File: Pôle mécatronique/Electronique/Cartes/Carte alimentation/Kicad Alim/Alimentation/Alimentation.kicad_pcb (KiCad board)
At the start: 2 copper layers, 11 parts, among them J1 Conn_01x04, J2 Conn_01x04, J3 Conn_01x04, J4 Conn_01x05, J5 Conn_02x03_Odd_Even, J6 Conn_01x05, K1 G5LE-1, Q1 2N7002, U1 TSR_2-2450, U2 TSR_2-2450, U3 TSR_2-24120

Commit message: Update alim
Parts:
- added D1: D, Diode_THT:D_DO-15_P12.70mm_Horizontal, F.Cu at (177.3, 89.4)
- added J7: Conn_02x10_Odd_Even, Connector_PinSocket_2.54mm:PinSocket_2x10_P2.54mm_Vertical, F.Cu at (131.8, 64.3)
- J5: footprint Connector_JST:JST_PH_B4B-PH-K_1x04_P2.00mm_Vertical -> Connector_Hirose:Hirose_DF11-6DP-2DSA_2x03_P2.00mm_Vertical
- Q1: value 2N7002 -> BSS138
- moved U2 54.2 mm to (140.5, 91.9), turned to 90 degrees
- moved J3 54.0 mm to (148.1, 42.4), turned to 270 degrees
- moved U1 52.1 mm to (129.3, 91.9), turned to 90 degrees
- moved J4 48.4 mm to (127.8, 42.4), turned to 270 degrees
- moved Q1 48.3 mm to (153.2, 74.2)
- moved J5 48.2 mm to (122.7, 73.4), turned to 180 degrees
- moved J2 43.5 mm to (157.0, 42.4), turned to 270 degrees
- moved J6 41.5 mm to (135.4, 42.4), turned to 270 degrees
- moved U3 28.0 mm to (151.9, 92.2), turned to 90 degrees
- moved J1 26.8 mm to (165.9, 42.4), turned to 270 degrees
- moved K1 20.1 mm to (165.9, 78.0)
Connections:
- J4 pad 4: 12Vout1 -> 5Vout4
- J6 pad 4: 12Vout2 -> 5Vout5
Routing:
- net GND: track 0.00 -> 135.1 mm
- net can_H: track 0.00 -> 95.1 mm
- net can_L: track 0.00 -> 90.8 mm
- net 5V: track 0.00 -> 71.5 mm
- net Net-(J7-Pad2): track 0.00 -> 49.6 mm
- net Vbatt: track 0.00 -> 43.2 mm
- net cmd_relais: track 0.00 -> 33.3 mm
- net Net-(J7-Pad16): track 0.00 -> 32.2 mm
- net 5VRPI: track 0.00 -> 30.4 mm
- net Net-(D1-Pad2): track 0.00 -> 27.9 mm
- net 5Vout1: track 0.00 -> 25.6 mm
- net VbattProtected: track 0.00 -> 21.9 mm
- net 5Vout4: track 0.00 -> 21.0 mm
- net 5Vout2: track 0.00 -> 21.0 mm
- net 5Vout3: track 0.00 -> 18.4 mm
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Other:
- board outline added: 71.1 x 66 mm

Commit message: Update alim
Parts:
- added J8: Conn_01x02, Connector_AMASS:AMASS_XT60-F_1x02_P7.20mm_Vertical, F.Cu at (116.3, 107.2)
- added R1: 6000, Resistor_THT:R_Axial_DIN0207_L6.3mm_D2.5mm_P10.16mm_Horizontal, F.Cu at (104.3, 60.8)
- added REF**: MountingHole_3.2mm_M3, MountingHole:MountingHole_3.2mm_M3, F.Cu at (90.9, 107.2)
- added REF**: MountingHole_3.2mm_M3, MountingHole:MountingHole_3.2mm_M3, F.Cu at (149.4, 107.2)
- added REF**: MountingHole_3.2mm_M3, MountingHole:MountingHole_3.2mm_M3, F.Cu at (90.9, 38.6)
- added REF**: MountingHole_3.2mm_M3, MountingHole:MountingHole_3.2mm_M3, F.Cu at (149.4, 38.6)
- Q1: moved to B.Cu
- moved D1 71.3 mm to (108.7, 69.7), turned to 180 degrees
- moved K1 63.6 mm to (102.4, 75.4)
- moved Q1 48.6 mm to (105.5, 64.6), turned to 270 degrees
- moved J5 35.4 mm to (97.9, 48.1), turned to 270 degrees
- moved U3 33.7 mm to (118.2, 91.9)
- moved J6 30.1 mm to (105.5, 46.2)
- moved J2 23.2 mm to (134.1, 46.2)
- moved J3 23.2 mm to (125.2, 46.2)
- moved J1 23.2 mm to (143.0, 46.2)
- moved J7 16.6 mm to (117.6, 72.9)
- moved J4 15.1 mm to (113.2, 46.2)
- moved U1 11.2 mm to (140.5, 91.9)
- moved U2 10.8 mm to (129.7, 91.9)
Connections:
- J5 pad 3: cmd_relais -> Net-(J5-Pad3)
- J5 pad 4: Net-(J5-Pad4) -> cmd_relais
- Q1 pad 1: cmd_relais -> Net-(Q1-Pad1)
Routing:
- net GND: track 135.1 -> 0.00 mm
- net 5VRPI: track 30.4 -> 90.3 mm, vias 0 -> 2
- net Net-(J7-Pad2): track 49.6 -> 14.2 mm
- net Vbatt: track 43.2 -> 69.1 mm
- net cmd_relais: track 33.3 -> 12.2 mm
- net can_H: track 95.1 -> 74.7 mm
- net 5V: track 71.5 -> 52.5 mm, vias 0 -> 2
- net Net-(J7-Pad16): track 32.2 -> 13.5 mm
- net can_L: track 90.8 -> 74.2 mm
- net 5Vout5: track 16.8 -> 28.6 mm
- net VbattProtected: track 21.9 -> 10.8 mm
- net 12Vout2: track 15.3 -> 24.3 mm
- net Net-(D1-Pad2): track 27.9 -> 19.2 mm
- net 5Vout4: track 21.0 -> 26.2 mm
- net 12Vout1: track 16.6 -> 21.6 mm, vias 0 -> 2
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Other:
- board size 71.1 x 66 mm -> 68.6 x 78.7 mm

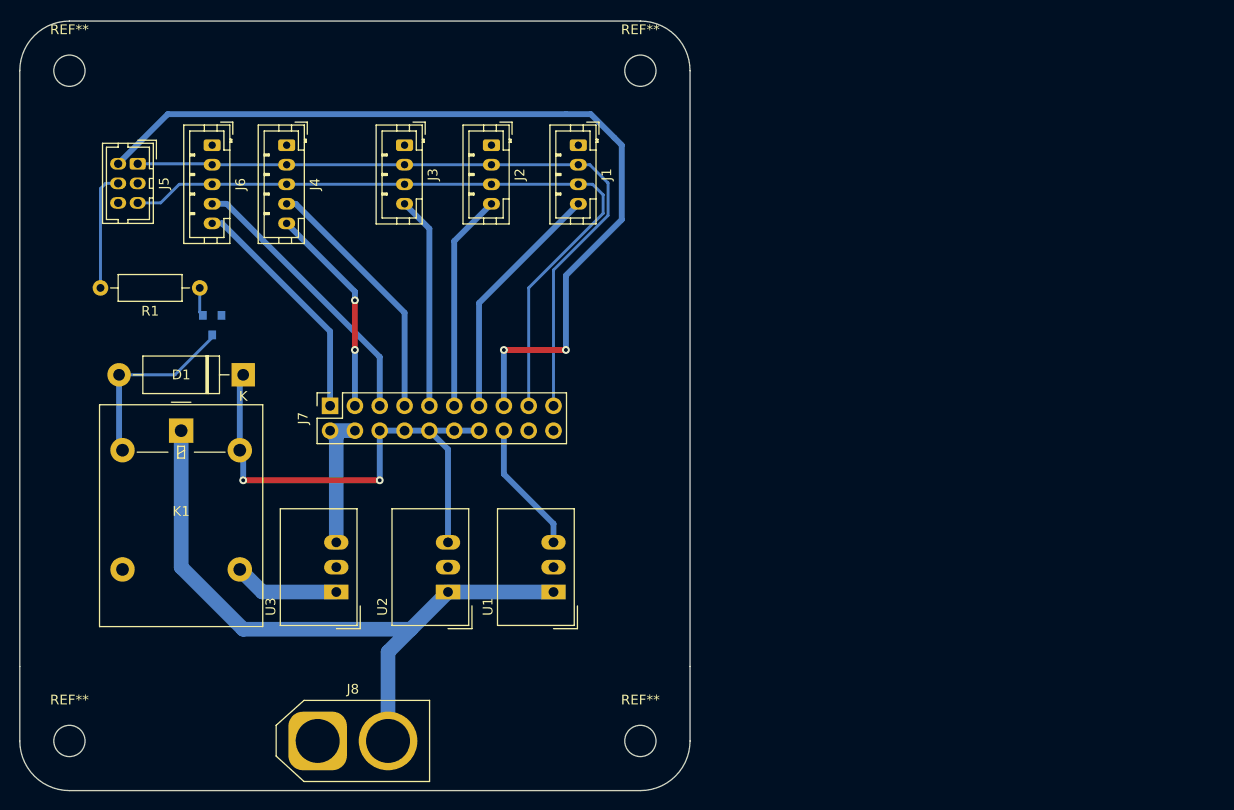
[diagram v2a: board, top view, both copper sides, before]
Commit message: Update Alim
Manque fusible
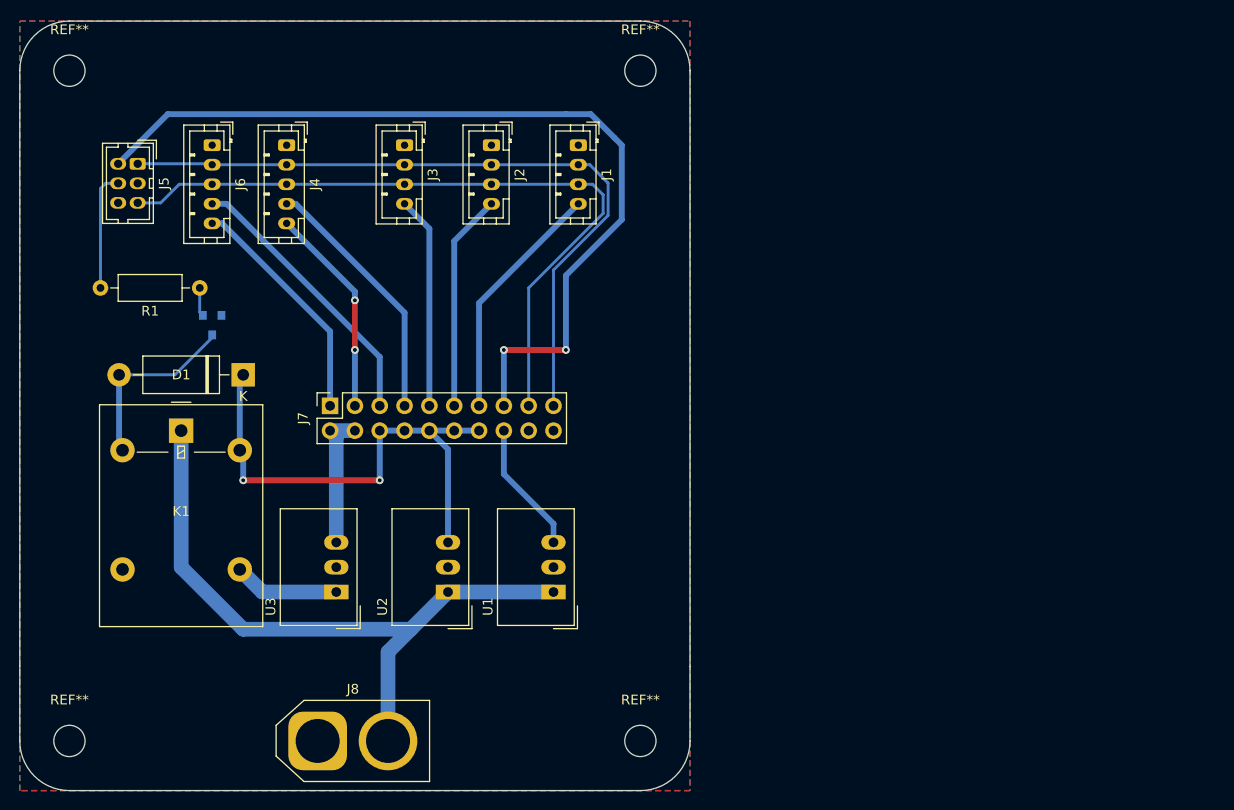
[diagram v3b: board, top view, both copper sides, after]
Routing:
- added copper zone on B.Cu, net GND
- added copper zone on F.Cu, net GND

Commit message: Update alim
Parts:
- added G***: LOGO, Logos:logoRobotechNancy10x10, F.Cu at (140.5, 60.2)
- added G***: LOGO, Logos:logoRobotechNancy10x10, B.Cu at (140.5, 60.2)
- added J9: Conn_01x02, Connector_AMASS:AMASS_XT60-F_1x02_P7.20mm_Vertical, F.Cu at (129.5, 107.2)
- Q1: value BSS138 -> BD135; footprint Package_TO_SOT_SMD:SOT-23 -> Package_TO_SOT_THT:TO-126-3_Vertical; moved to F.Cu
- R1: value 6000 -> 18000
- moved J8 11.2 mm to (105.1, 107.2)
- moved Q1 6.36 mm to (99.2, 64.4), turned to 0 degrees
- moved R1 1.91 mm to (104.3, 58.9)
- moved J4 0.64 mm to (113.8, 46.2)
- renumbered J6 to J5, J5 to J6
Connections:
- J6 pad 3: Net-(J5-Pad3) -> can_L
- J6 pad 5: can_L -> unconnected-(J6-Pad5)
- J7 pad 20: Net-(J7-Pad20) -> unconnected-(J7-Pad20)
- K1 pad 3: Net-(K1-Pad3) -> unconnected-(K1-Pad3)
- Q1 pad 1: Net-(Q1-Pad1) -> GND
- Q1 pad 2: GND -> Net-(D1-Pad2)
- Q1 pad 3: Net-(D1-Pad2) -> Net-(R1-Pad1)
- R1 pad 1: Net-(Q1-Pad1) -> Net-(R1-Pad1)
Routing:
- net Vbatt: track 69.1 -> 84.8 mm
- net Net-(R1-Pad1): track 0.00 -> 5.45 mm
- net Net-(Q1-Pad1): track 2.94 -> 0.00 mm
- net Net-(D1-Pad2): track 19.2 -> 17.1 mm
- net cmd_relais: track 12.2 -> 10.3 mm
- net can_L: track 74.2 -> 73.5 mm
- net 5Vout4: track 26.2 -> 25.6 mm
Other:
- net class Default removed
- board text added: "+"
- board text added: "-"
- board text added: "-12V"
- board text added: "-5V"
- board text added: "-5VRPI"
- board text added: "12V"
- board text added: "5V"
- board text added: "5V-12V"
- board text added: "5VRPI"
- board text added: "Batterie"
- board text added: "Carte de mesure"
- board text added: "GND"
- board text added: "ROBOTECH NANCY"
- board text added: "Relais"
- board text added: "canH"
- board text added: "canL"

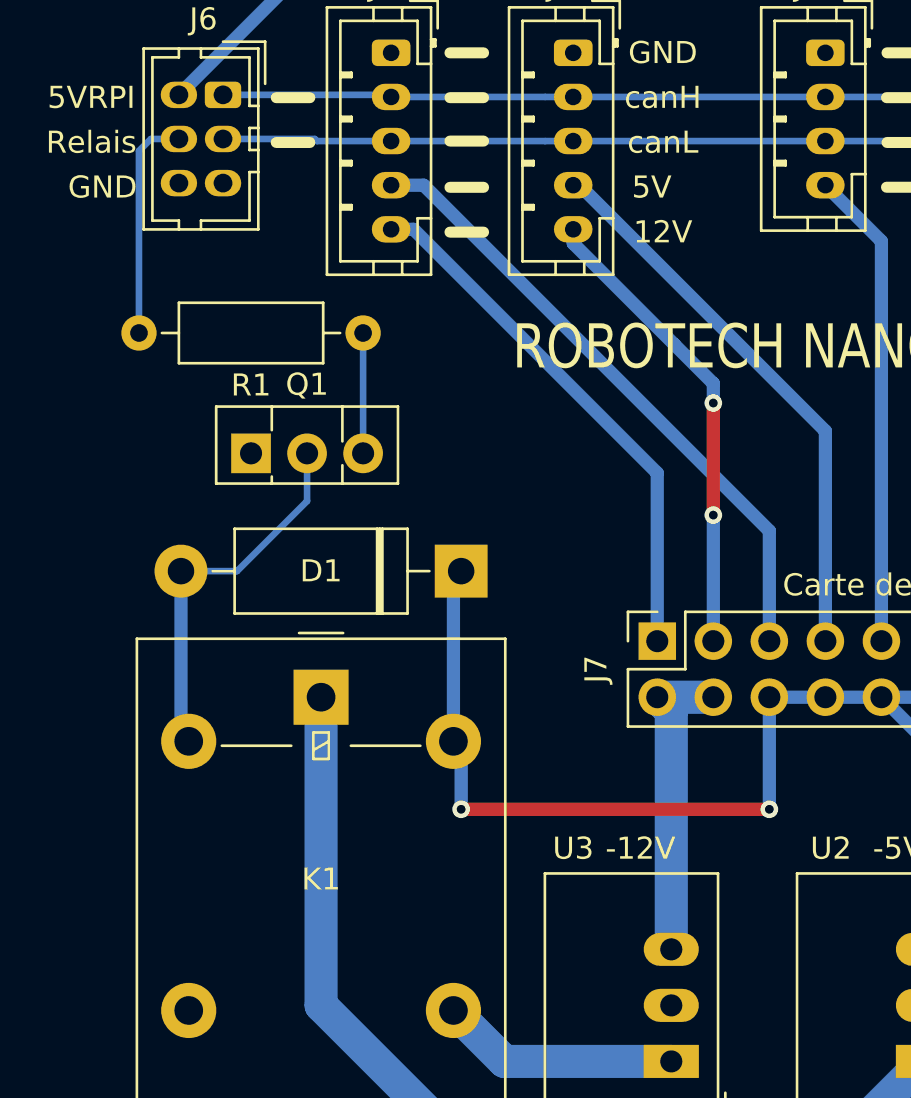
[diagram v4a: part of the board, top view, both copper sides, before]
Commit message: Update Alim
Transistor alimenté en 12V
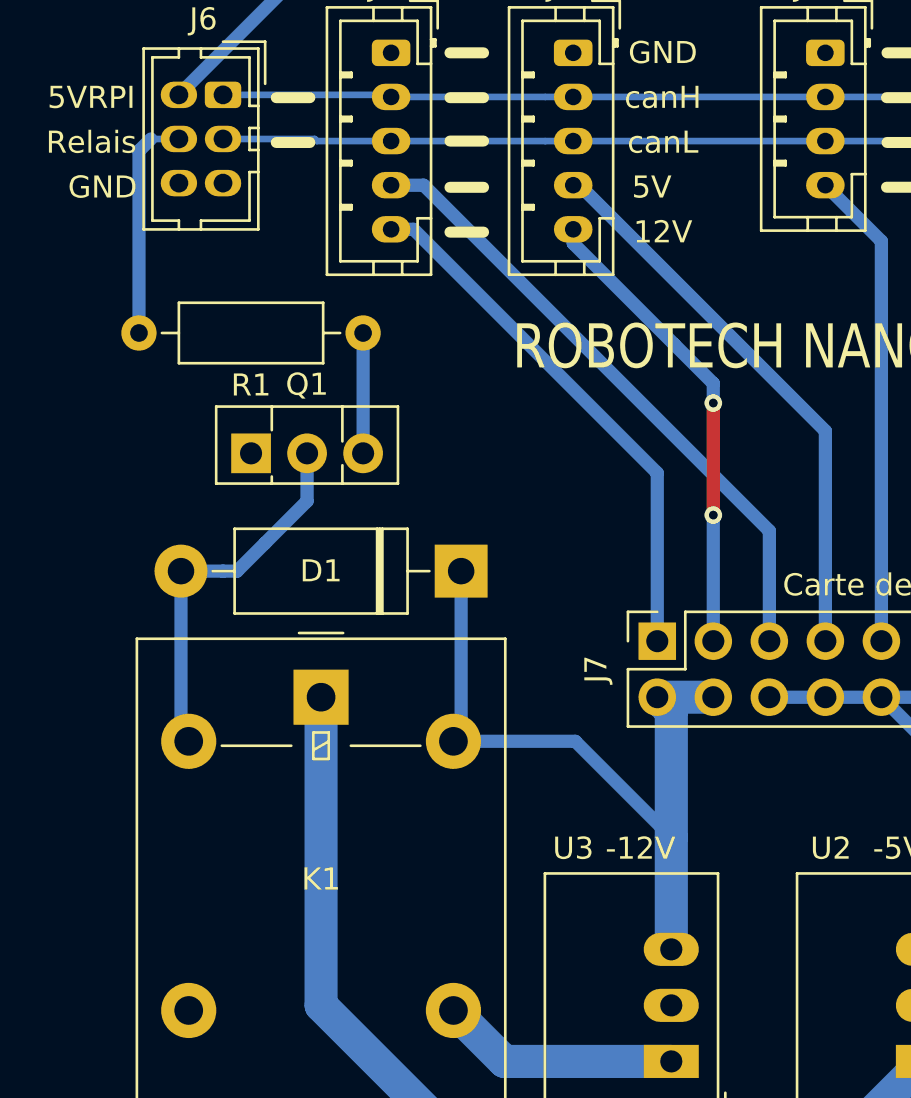
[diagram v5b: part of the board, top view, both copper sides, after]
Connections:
- D1 pad 1: 5V -> 12V
- J7 pad 2: Net-(J7-Pad2) -> 12V
- J7 pad 4: Net-(J7-Pad2) -> 12V
- K1 pad 5: 5V -> 12V
- U3 pad 3: Net-(J7-Pad2) -> 12V
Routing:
- net 12V: track 0.00 -> 34.3 mm
- net 5V: track 52.5 -> 22.4 mm, vias 2 -> 0
- net Net-(J7-Pad2): track 14.2 -> 0.00 mm
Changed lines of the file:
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@@
   (net 13 "Net-(D1-Pad2)")
   (net 14 "Vbatt")
-  (net 15 "Net-(J7-Pad2)")
+  (net 15 "12V")
   (net 16 "5Vout4")
   (net 17 "5Vout5")
@@
   (net 20 "unconnected-(K1-Pad3)")
   (net 21 "unconnected-(J6-Pad5)")
-  (net 22 "Net-(R1-Pad1)")
+  (net 22 "Net-(Q1-Pad3)")
   (footprint "Connector_JST:JST_PH_B4B-PH-K_1x04_P2.00mm_Vertical" (layer "F.Cu")
     (at 143.002 46.228 -90)
@@
       (net 12 "VbattProtected") (pintype "passive"))
     (pad "5" thru_hole oval locked (at 6 2) (size 2.5 2.5) (drill 1.3) (layers *.Cu *.Mask)
-      (net 11 "5V") (pintype "passive"))
+      (net 15 "12V") (pintype "passive"))
     (model "${KICAD6_3DMODEL_DIR}/Relay_THT.3dshapes/Relay_SPDT_Omron-G5LE-1.wrl"
       (offset (xyz 0 0 0))
@@
       (net 4 "GND") (pinfunction "GND") (pintype "power_in"))
     (pad "3" thru_hole oval locked (at 5.08 0 90) (size 1.5 2.5) (drill 1) (layers *.Cu *.Mask)
-      (net 15 "Net-(J7-Pad2)") (pinfunction "Vout") (pintype "power_out"))
+      (net 15 "12V") (pinfunction "Vout") (pintype "power_out"))
     (model "${KICAD6_3DMODEL_DIR}/Converter_DCDC.3dshapes/Converter_DCDC_TRACO_TSR-1_THT.wrl"
       (offset (xyz 0 0 0))
@@
       (net 10 "12Vout2") (pinfunction "Pin_1") (pintype "passive"))
     (pad "2" thru_hole oval locked (at -2.54 0 90) (size 1.7 1.7) (drill 1) (layers *.Cu *.Mask)
-      (net 15 "Net-(J7-Pad2)") (pinfunction "Pin_2") (pintype "passive"))
+      (net 15 "12V") (pinfunction "Pin_2") (pintype "passive"))
     (pad "3" thru_hole oval locked (at 0 2.54 90) (size 1.7 1.7) (drill 1) (layers *.Cu *.Mask)
       (net 7 "12Vout1") (pinfunction "Pin_3") (pintype "passive"))
     (pad "4" thru_hole oval locked (at -2.54 2.54 90) (size 1.7 1.7) (drill 1) (layers *.Cu *.Mask)
-      (net 15 "Net-(J7-Pad2)") (pinfunction "Pin_4") (pintype "passive"))
+      (net 15 "12V") (pinfunction "Pin_4") (pintype "passive"))
     (pad "5" thru_hole oval locked (at 0 5.08 90) (size 1.7 1.7) (drill 1) (layers *.Cu *.Mask)
       (net 17 "5Vout5") (pinfunction "Pin_5") (pintype "passive"))
@@
     (fp_line (start 2.55 1.8) (end 10.15 1.8) (layer "F.Fab") (width 0.1))
     (pad "1" thru_hole rect locked (at 0 0 180) (size 2.4 2.4) (drill 1.2) (layers *.Cu *.Mask)
-      (net 11 "5V") (pinfunction "K") (pintype "passive"))
+      (net 15 "12V") (pinfunction "K") (pintype "passive"))
     (pad "2" thru_hole oval locked (at 12.7 0 180) (size 2.4 2.4) (drill 1.2) (layers *.Cu *.Mask)
       (net 13 "Net-(D1-Pad2)") (pinfunction "A") (pintype "passive"))
@@
     (fp_line (start 8.23 1.25) (end 8.23 -1.25) (layer "F.Fab") (width 0.1))
     (pad "1" thru_hole circle locked (at 0 0 180) (size 1.6 1.6) (drill 0.8) (layers *.Cu *.Mask)
-      (net 22 "Net-(R1-Pad1)") (pintype "passive"))
+      (net 22 "Net-(Q1-Pad3)") (pintype "passive"))
     (pad "2" thru_hole oval locked (at 10.16 0 180) (size 1.6 1.6) (drill 0.8) (layers *.Cu *.Mask)
       (net 8 "cmd_relais") (pintype "passive"))
@@
       (net 13 "Net-(D1-Pad2)") (pinfunction "C") (pintype "passive"))
     (pad "3" thru_hole oval locked (at 5.08 0) (size 1.8 1.8) (drill 1) (layers *.Cu *.Mask)
-      (net 22 "Net-(R1-Pad1)") (pinfunction "B") (pintype "input"))
+      (net 22 "Net-(Q1-Pad3)") (pinfunction "B") (pintype "input"))
     (model "${KICAD6_3DMODEL_DIR}/Package_TO_SOT_THT.3dshapes/TO-126-3_Vertical.wrl"
       (offset (xyz 0 0 0))
@@
   (segment (start 120.142 72.898) (end 120.142 67.183) (width 0.6) (layer "B.Cu") (net 7))
   (segment (start 118.3645 59.4355) (end 113.792 54.863) (width 0.6) (layer "B.Cu") (net 7))
-  (segment (start 94.107 58.928) (end 94.107 50.673) (width 0.3) (layer "B.Cu") (net 8))
   (segment (start 94.647 50.133) (end 95.917 50.133) (width 0.3) (layer "B.Cu") (net 8))
-  (segment (start 94.107 50.673) (end 94.647 50.133) (width 0.3) (layer "B.Cu") (net 8))
+  (segment (start 94.107 50.673) (end 94.107 58.928) (width 0.6) (layer "B.Cu") (net 8))
+  (segment (start 94.647 50.133) (end 94.107 50.673) (width 0.6) (layer "B.Cu") (net 8))
   (segment (start 141.732 67.183) (end 135.382 67.183) (width 0.6) (layer "F.Cu") (net 9))
   (via (at 135.382 67.183) (size 0.8) (drill 0.4) (layers "F.Cu" "B.Cu") (net 9))
@@
   (segment (start 117.602 72.898) (end 117.602 65.278) (width 0.6) (layer "B.Cu") (net 10))
   (segment (start 106.552 54.228) (end 105.537 54.228) (width 0.6) (layer "B.Cu") (net 10))
-  (segment (start 108.712 80.518) (end 122.682 80.518) (width 0.6) (layer "F.Cu") (net 11))
-  (via (at 122.682 80.518) (size 0.8) (drill 0.4) (layers "F.Cu" "B.Cu") (net 11))
-  (via (at 108.712 80.518) (size 0.8) (drill 0.4) (layers "F.Cu" "B.Cu") (net 11))
   (segment (start 125.222 75.438) (end 122.682 75.438) (width 0.6) (layer "B.Cu") (net 11))
   (segment (start 132.842 75.438) (end 130.302 75.438) (width 0.6) (layer "B.Cu") (net 11))
   (segment (start 127.762 75.438) (end 125.222 75.438) (width 0.6) (layer "B.Cu") (net 11))
-  (segment (start 108.362 77.438) (end 108.362 70.073) (width 0.6) (layer "B.Cu") (net 11))
-  (segment (start 108.712 77.788) (end 108.362 77.438) (width 0.6) (layer "B.Cu") (net 11))
-  (segment (start 108.362 70.073) (end 108.712 69.723) (width 0.6) (layer "B.Cu") (net 11))
   (segment (start 129.667 77.343) (end 127.762 75.438) (width 0.6) (layer "B.Cu") (net 11))
-  (segment (start 122.682 75.438) (end 122.682 80.518) (width 0.6) (layer "B.Cu") (net 11))
   (segment (start 130.302 75.438) (end 127.762 75.438) (width 0.6) (layer "B.Cu") (net 11))
-  (segment (start 108.712 80.518) (end 108.712 77.788) (width 0.6) (layer "B.Cu") (net 11))
   (segment (start 129.667 86.868) (end 129.667 77.343) (width 0.6) (layer "B.Cu") (net 11))
   (segment (start 118.237 91.948) (end 110.672 91.948) (width 1.5) (layer "B.Cu") (net 12))
   (segment (start 110.672 91.948) (end 108.362 89.638) (width 1.5) (layer "B.Cu") (net 12))
-  (segment (start 98.552 69.723) (end 96.012 69.723) (width 0.3) (layer "B.Cu") (net 13))
-  (segment (start 101.727 66.548) (end 98.552 69.723) (width 0.3) (layer "B.Cu") (net 13))
+  (segment (start 99.822 68.453) (end 98.552 69.723) (width 0.6) (layer "B.Cu") (net 13))
   (segment (start 96.012 77.088) (end 96.362 77.438) (width 0.6) (layer "B.Cu") (net 13))
-  (segment (start 101.727 64.383) (end 101.727 66.548) (width 0.3) (layer "B.Cu") (net 13))
+  (segment (start 101.727 66.548) (end 99.822 68.453) (width 0.6) (layer "B.Cu") (net 13))
+  (segment (start 101.727 64.383) (end 101.727 66.548) (width 0.6) (layer "B.Cu") (net 13))
+  (segment (start 96.012 69.723) (end 97.917 69.723) (width 0.6) (layer "B.Cu") (net 13))
+  (segment (start 98.552 69.723) (end 97.917 69.723) (width 0.6) (layer "B.Cu") (net 13))
   (segment (start 96.012 69.723) (end 96.012 77.088) (width 0.6) (layer "B.Cu") (net 13))
   (segment (start 112.312 107.188) (end 112.312 99.358) (width 1.5) (layer "B.Cu") (net 14))
@@
   (segment (start 108.712 95.758) (end 125.857 95.758) (width 1.5) (layer "B.Cu") (net 14))
   (segment (start 102.362 75.438) (end 102.362 89.408) (width 1.5) (layer "B.Cu") (net 14))
-  (segment (start 118.237 86.868) (end 118.237 76.073) (width 1.5) (layer "B.Cu") (net 15))
+  (segment (start 118.237 81.788) (end 118.237 76.073) (width 1.5) (layer "B.Cu") (net 15))
+  (segment (start 113.887 77.438) (end 118.237 81.788) (width 0.6) (layer "B.Cu") (net 15))
+  (segment (start 108.712 77.788) (end 108.362 77.438) (width 0.6) (layer "B.Cu") (net 15))
+  (segment (start 108.362 77.438) (end 113.887 77.438) (width 0.6) (layer "B.Cu") (net 15))
   (segment (start 117.602 75.438) (end 120.142 75.438) (width 1.5) (layer "B.Cu") (net 15))
+  (segment (start 118.237 86.868) (end 118.237 81.788) (width 1.5) (layer "B.Cu") (net 15))
+  (segment (start 108.712 77.088) (end 108.362 77.438) (width 0.6) (layer "B.Cu") (net 15))
   (segment (start 118.237 76.073) (end 117.602 75.438) (width 1.5) (layer "B.Cu") (net 15))
+  (segment (start 108.712 69.723) (end 108.712 77.088) (width 0.6) (layer "B.Cu") (net 15))
   (segment (start 125.222 63.373) (end 114.077 52.228) (width 0.6) (layer "B.Cu") (net 16))
   (segment (start 125.222 72.898) (end 125.222 63.373) (width 0.6) (layer "B.Cu") (net 16))
@@
   (segment (start 140.462 84.963) (end 135.382 79.883) (width 0.6) (layer "B.Cu") (net 18))
   (segment (start 135.382 79.883) (end 135.382 75.438) (width 0.6) (layer "B.Cu") (net 18))
-  (segment (start 104.267 64.383) (end 104.267 58.928) (width 0.3) (layer "B.Cu") (net 22))
+  (segment (start 104.267 58.928) (end 104.267 64.383) (width 0.6) (layer "B.Cu") (net 22))
   (zone (net 4) (net_name "GND") (layer "F.Cu") (hatch edge 0.508)
     (connect_pads (clearance 0.608))
